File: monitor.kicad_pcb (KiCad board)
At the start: 4 copper layers, 35.5 x 33.7 mm, 54 parts, among them J1 USB_C_Plug, J2 USB_C_Receptacle_USB2.0_14P, J3 Display, J4 Program, J5 Boot, U1 STM32U031K8Ux, U2 TPSM365R6V3RDNR, U3 TMP117xxDRV, U4 REF5025ADGK, U5 CC6903, Y1 32768Hz

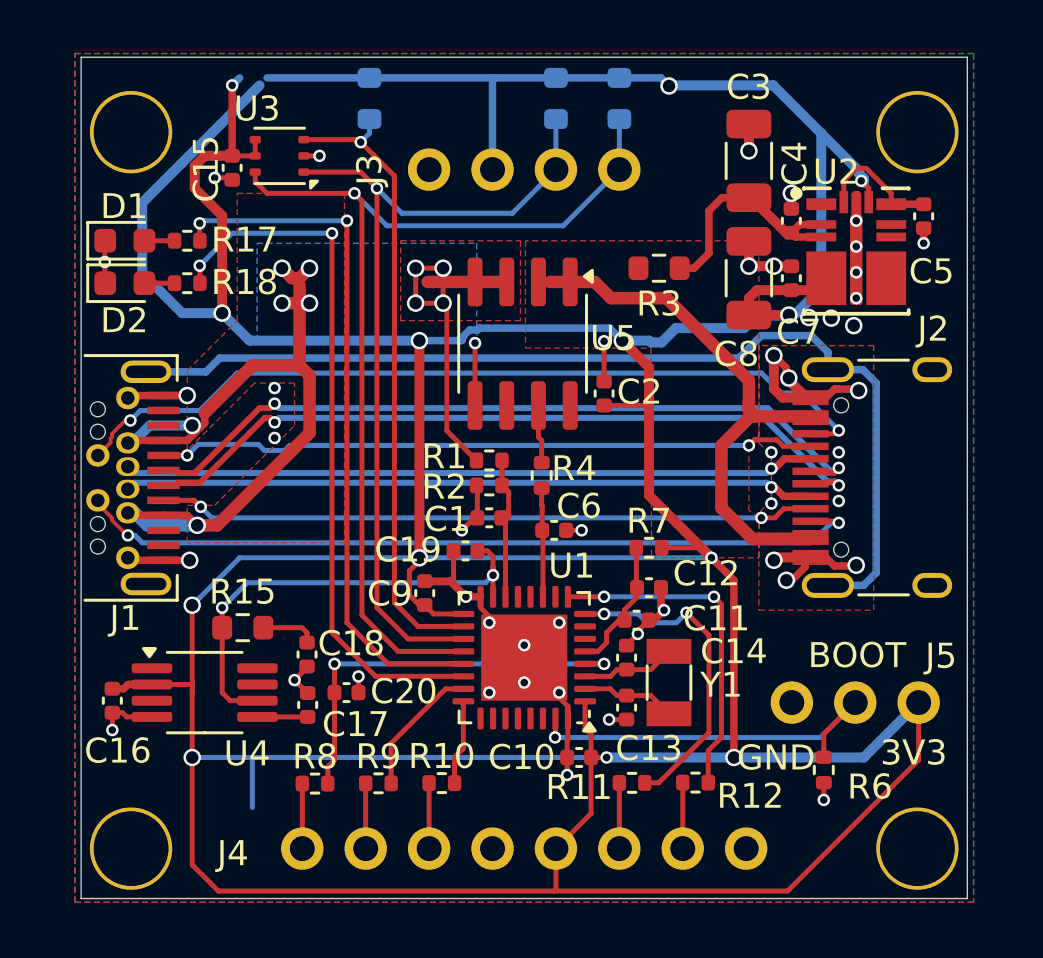
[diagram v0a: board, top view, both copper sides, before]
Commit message: Big update to the monitor.
Accell, low side current sense.
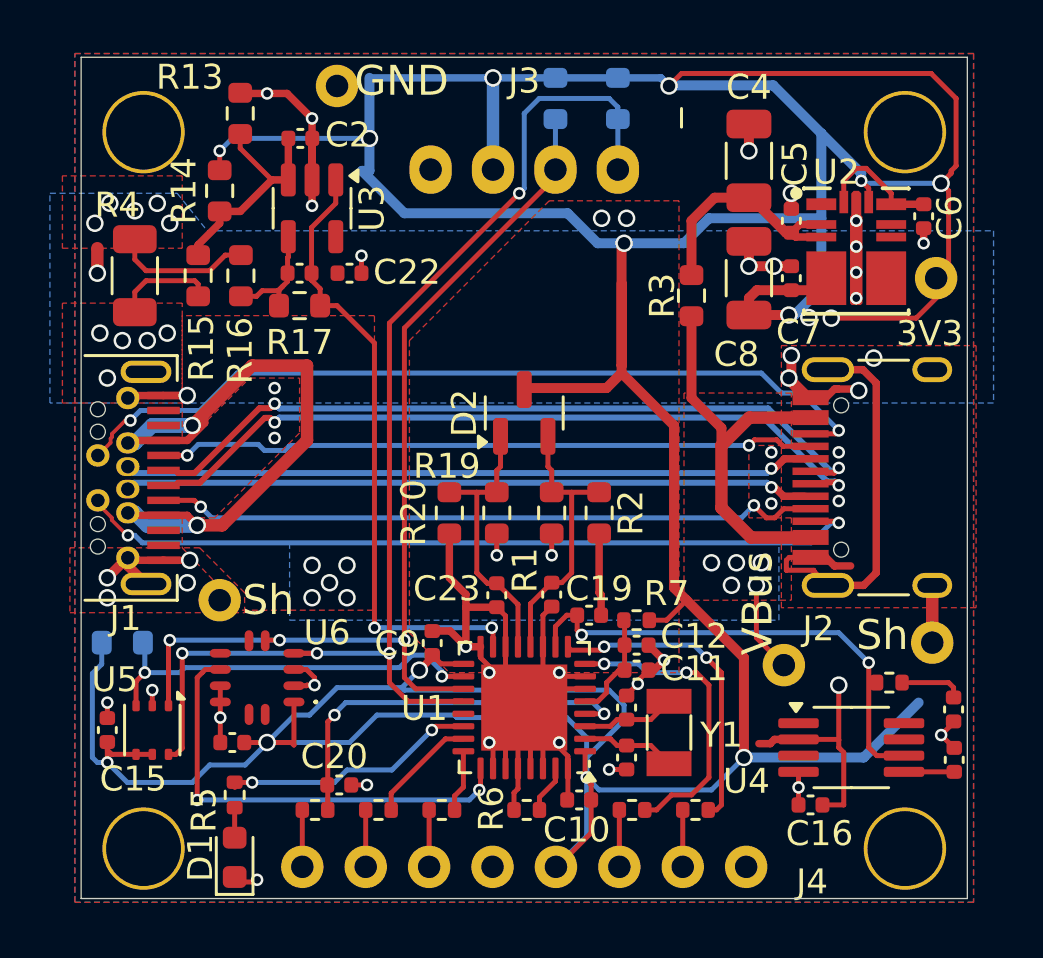
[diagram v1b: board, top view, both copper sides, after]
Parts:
- removed the C6 at (101.2, 102.1)
- removed J5: Boot, Parts:PinHeader_1x03_P2.54mm_Vertical
- removed the R18 at (86.5, 92.2)
- removed the U5 at (99.9, 94.6)
- added C21: 1u, Capacitor_SMD:C_0402_1005Metric, F.Cu at (88.3, 110.6)
- added C22: 0u1, Capacitor_SMD:C_0402_1005Metric, F.Cu at (93.0, 91.8)
- added C23: 4u7, Capacitor_SMD:C_0402_1005Metric, F.Cu at (98.9, 104.7)
- added C3: 1u, Capacitor_SMD:C_0402_1005Metric, F.Cu at (91.0, 91.8)
- added NT1: NetTie_2, Parts:NetTie-2_0.2mm, F.Cu at (84.4, 92.7)
- added NT2: NetTie_2, Parts:NetTie-2_0.2mm, F.Cu at (84.4, 91.1)
- added NT3: NetTie_2, NetTie:NetTie-2_SMD_Pad0.5mm, F.Cu at (82.9, 91.3)
- added R13: 200k, Resistor_SMD:R_0603_1608Metric, F.Cu at (88.6, 85.4)
- added R14: 200k, Resistor_SMD:R_0603_1608Metric, F.Cu at (87.8, 88.5)
- added R15: 390, Resistor_SMD:R_0603_1608Metric, F.Cu at (86.9, 91.9)
- added R16: 390, Resistor_SMD:R_0603_1608Metric, F.Cu at (88.7, 91.9)
- added R17: 100k, Resistor_SMD:R_0603_1608Metric, F.Cu at (91.0, 93.1)
- added R19: 330k, Resistor_SMD:R_0603_1608Metric, F.Cu at (98.9, 101.4)
- added R20: 22k, Resistor_SMD:R_0603_1608Metric, F.Cu at (97.0, 101.4)
- added TP1: TestPoint, Parts:TestPoint, F.Cu at (87.8, 104.9)
- added TP2: TestPoint, Parts:TestPoint, F.Cu at (116.3, 106.6)
- added TP3: TestPoint, Parts:TestPoint, F.Cu at (110.4, 107.5)
- added TP4: TestPoint, Parts:TestPoint, F.Cu at (92.5, 84.3)
- added TP5: TestPoint, Parts:TestPoint, F.Cu at (116.5, 92.0)
- added U3: OPA388, Package_TO_SOT_SMD:SOT-23-5, F.Cu at (91.5, 89.2)
- added U6: FXLS8971CF, Parts:FXLS8971CF, F.Cu at (89.3, 108.0)
- C1: value 10u -> 1u
- C2: value 0u1 -> 1u
- C20: value 0u1 -> 100p
- D2: value Red -> BAV70; footprint LED_SMD:LED_0603_1608Metric -> Package_TO_SOT_SMD:SOT-23
- H1, H3, H4: moved to B.Cu
- J3: footprint Parts:PinHeader_1x04_P2.54mm_Vertical -> Parts:JST_XH_B4B-XH-A_1x04_P2.50mm_Vertical
- R1: value 100k -> 220k; footprint Resistor_SMD:R_0402_1005Metric -> Resistor_SMD:R_0603_1608Metric
- R18: renamed from R15; footprint Resistor_SMD:R_0603_1608Metric -> Resistor_SMD:R_0402_1005Metric
- R2: value 18k -> 100k; footprint Resistor_SMD:R_0402_1005Metric -> Resistor_SMD:R_0603_1608Metric
- R4: value 220 -> 1m; footprint Resistor_SMD:R_0402_1005Metric -> Resistor_SMD:R_1206_3216Metric
- moved C16 28.3 mm to (111.5, 113.1), turned to 180 degrees
- moved C18 26.0 mm to (117.2, 109.3)
- moved R18 26.0 mm to (114.6, 108.2)
- moved C17 26.0 mm to (117.2, 111.3)
- moved U4 26.0 mm to (113.1, 110.8)
- moved D1 25.1 mm to (88.4, 115.2), turned to 90 degrees
- moved R33 23.9 mm to (83.9, 106.6), turned to 0 degrees
- moved U5 23.6 mm to (85.1, 110.1), turned to -90 degrees
- moved C15 23.1 mm to (83.3, 110.1), turned to 90 degrees
- moved R5 22.3 mm to (88.4, 112.7), turned to -90 degrees
- moved R4 18.2 mm to (84.4, 91.9), turned to -90 degrees
- moved D2 16.8 mm to (100.0, 97.4), turned to 90 degrees
- moved C2 15.9 mm to (91.0, 86.4), turned to 180 degrees
- moved R6 12.0 mm to (100.1, 113.3), turned to 0 degrees
- moved C19 5.58 mm to (102.6, 105.5), turned to 0 degrees
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- renumbered C3 to C4, C4 to C5, C5 to C6, R13 to R31, R14 to R32, R5 to R33, R17 to R5, U3 to U5
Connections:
- C1 pad 1: /VSense -> /VSense1
- C2 pad 1: +3V3 -> GND
- C2 pad 2: GND -> Net-(U3-+)
- D2 pad 1: GND -> /VSense2
- D2 pad 2: Net-(D2-A) -> /VSense1
- J1 pad A1: GND -> /MGnd
- J1 pad A12: GND -> /MGnd
- J1 pad A4: /Vout -> /VBus
- J1 pad A9: /Vout -> /VBus
- J1 pad B1: GND -> /MGnd
- J1 pad B12: GND -> /MGnd
- J1 pad B4: /Vout -> /VBus
- J1 pad B9: /Vout -> /VBus
- J1 pad S1: unconnected-(J1-SHIELD-PadS1) -> /MGnd
- J1 pad S2: Earth -> /MGnd
- J2 pad A1: GND -> /UGnd
- J2 pad A12: GND -> /UGnd
- J2 pad B1: GND -> /UGnd
- J2 pad B12: GND -> /UGnd
- J2 pad S1: Earth -> /UGnd
- J2 pad S2: unconnected-(J2-SHIELD-PadS2) -> /UGnd
- J2 pad S3: unconnected-(J2-SHIELD-PadS3) -> /UGnd
- J2 pad S4: Earth -> /UGnd
- R1 pad 1: /Vout -> /VBus
- R1 pad 2: /VSense -> /VSense1
- R2 pad 1: /VSense -> GND
- R2 pad 2: GND -> /VSense1
- R4 pad 1: /ISense -> /UGnd
- R4 pad 2: Net-(U5-VIOUT) -> /MGnd
- R5 pad 1: /Green -> /White
- R6 pad 1: /BOOT0 -> GND
- R6 pad 2: GND -> /BOOT0
- U1 pad 10: unconnected-(U1-PA4-Pad10) -> /VRef
- U1 pad 11: /ISense -> GND
- U1 pad 12: unconnected-(U1-PA6-Pad12) -> /VSense1
- U1 pad 13: unconnected-(U1-PA7-Pad13) -> /VSense2
- U1 pad 14: /VSense -> GND
- U1 pad 15: /VRef -> /ISense
- U1 pad 21: /Green -> unconnected-(U1-PA11-Pad21)
- U1 pad 22: /Red -> /White
- U1 pad 25: unconnected-(U1-PA15-Pad25) -> /AccInt
- U1 pad 26: unconnected-(U1-PB3-Pad26) -> GND
- U1 pad 27: unconnected-(U1-PB4-Pad27) -> GND
- U1 pad 28: unconnected-(U1-PB5-Pad28) -> GND
- U1 pad 29: unconnected-(U1-PB6-Pad29) -> GND
- U1 pad 30: unconnected-(U1-PB7-Pad30) -> GND
- U1 pad 6: unconnected-(U1-PA0-Pad6) -> GND
- U1 pad 7: unconnected-(U1-PA1-Pad7) -> GND
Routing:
- net /Vout: track 46.4 -> 0.00 mm, vias 10 -> 0
- net Earth: track 40.8 -> 0.00 mm
- net /Red: track 28.5 -> 0.00 mm, vias 2 -> 0
- net /Green: track 28.1 -> 0.00 mm, vias 2 -> 0
- net /VBus: track 21.8 -> 48.3 mm, vias 0 -> 14
- net /MGnd: track 0.00 -> 26.4 mm, vias 0 -> 10
- net /UGnd: track 0.00 -> 24.6 mm, vias 0 -> 9
- net GND: track 48.1 -> 71.6 mm, vias 45 -> 38
- net /ISense: track 4.33 -> 25.3 mm, vias 0 -> 2
- net /AccInt: track 0.00 -> 18.3 mm, vias 0 -> 2
- net +3V3: track 240.0 -> 222.2 mm
- net /BOOT0: track 16.1 -> 1.93 mm, vias 1 -> 0
- net /VSense1: track 0.00 -> 11.1 mm
- net /VSense2: track 0.00 -> 11.1 mm
- net /White: track 0.00 -> 10.1 mm, vias 0 -> 2
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- added copper zone on F.Cu, net /MGnd
- added copper zone on In1.Cu, net /MGnd
- added copper zone on B.Cu, net /UGnd
- added copper zone on F.Cu, net /UGnd
- added copper zone on B.Cu, net /VBus
- removed copper zone on B.Cu, net /Vout
- removed copper zone on F.Cu, net /Vout
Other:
- board text added: "Sh"
- board text added: "VBus"
- board text removed: "BOOT"

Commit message: Switch to the 2-stage sense amp.
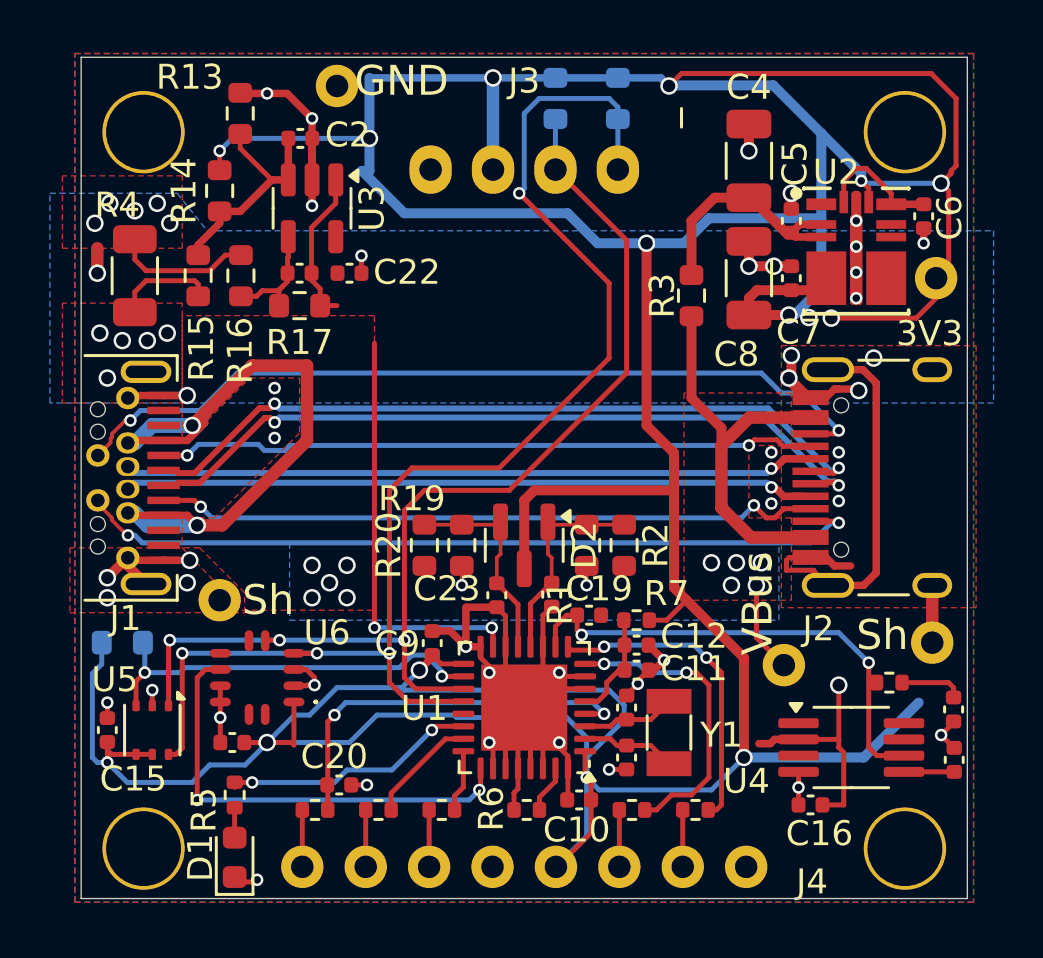
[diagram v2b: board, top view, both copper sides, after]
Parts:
- moved D2 5.30 mm to (100.0, 102.7), turned to -90 degrees
- moved R1 1.91 mm to (102.5, 102.7)
- moved R19 1.91 mm to (97.5, 102.7)
- moved R2 1.64 mm to (104.0, 102.7)
- moved R20 1.64 mm to (96.0, 102.7)
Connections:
- D2 pad 1: /VSense2 -> /VSense1
- D2 pad 2: /VSense1 -> /VSense2
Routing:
- net GND: track 71.6 -> 65.2 mm, vias 38 -> 36
- net /SDA: track 48.6 -> 53.6 mm
- net /SCL: track 40.1 -> 44.4 mm
- net /VSense1: track 11.1 -> 8.51 mm
- net /VSense2: track 11.1 -> 8.51 mm
- net /ISense: track 25.3 -> 23.1 mm
- net +3V3: track 222.2 -> 223.1 mm
- removed copper zone on F.Cu, net GND

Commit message: Board layout updated.
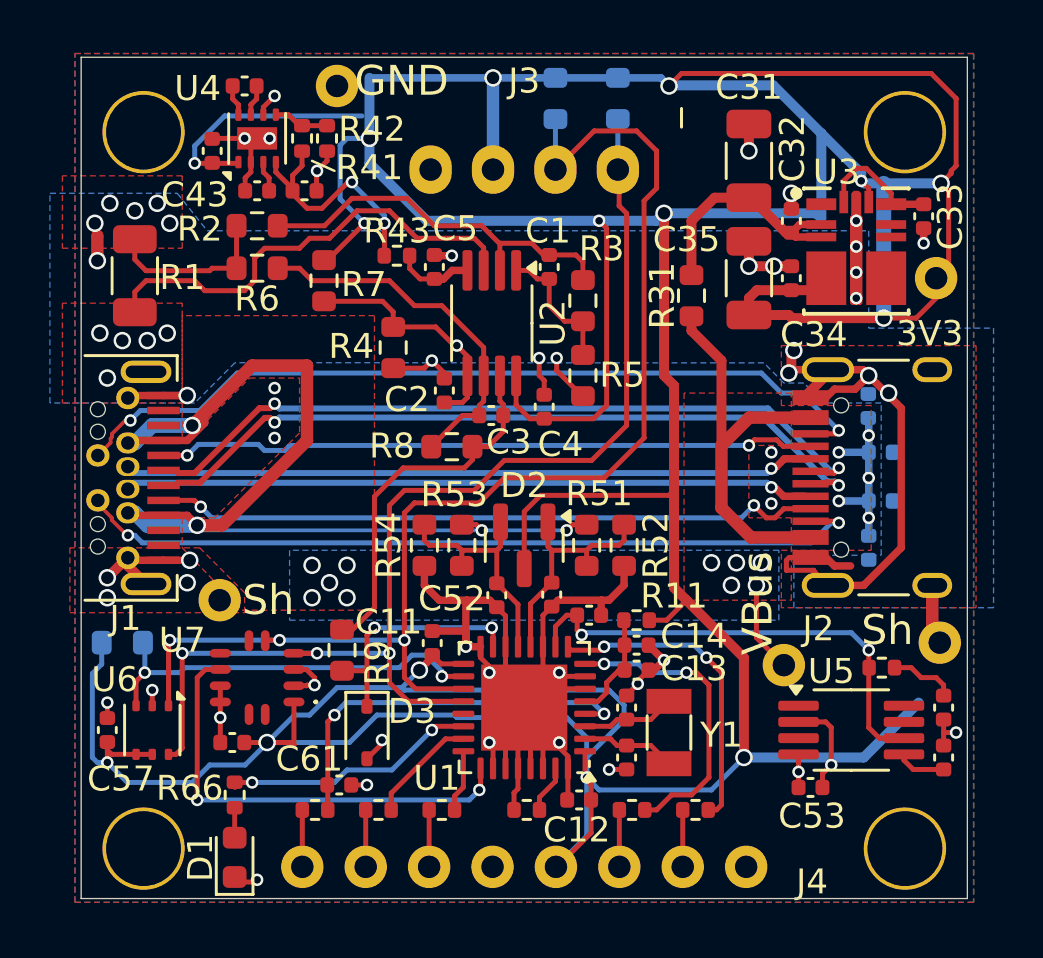
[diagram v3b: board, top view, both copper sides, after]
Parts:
- removed C22: 0u1, Capacitor_SMD:C_0402_1005Metric
- removed R15, R16: 390, Resistor_SMD:R_0603_1608Metric
- removed the U3 at (91.5, 89.2)
- added C2: 1u, Capacitor_SMD:C_0402_1005Metric, F.Cu at (96.8, 96.5)
- added C4: 0u1, Capacitor_SMD:C_0402_1005Metric, F.Cu at (100.8, 97.2)
- added C41: 4u7, Capacitor_SMD:C_0402_1005Metric, F.Cu at (87.5, 86.9)
- added C42: 1u, Capacitor_SMD:C_0402_1005Metric, F.Cu at (88.8, 84.3)
- added C43: 4u7, Capacitor_SMD:C_0402_1005Metric, F.Cu at (89.3, 88.5)
- added C44: 4u7, Capacitor_SMD:C_0402_1005Metric, F.Cu at (91.2, 88.5)
- added C5: 0u1, Capacitor_SMD:C_0402_1005Metric, F.Cu at (96.4, 91.5)
- added C91: 0u1, Capacitor_SMD:C_0402_1005Metric, B.Cu at (113.8, 102.8)
- added C92: 0u1, Capacitor_SMD:C_0402_1005Metric, B.Cu at (114.3, 99.0)
- added C93: 0u1, Capacitor_SMD:C_0402_1005Metric, B.Cu at (114.3, 100.9)
- added C94: 0u1, Capacitor_SMD:C_0402_1005Metric, B.Cu at (113.8, 97.1)
- added D3: 1N5819, Diode_SMD:D_SOD-323, F.Cu at (93.7, 110.2)
- added R2: 1k, Resistor_SMD:R_0603_1608Metric, F.Cu at (89.3, 89.9)
- added R41: 200k, Resistor_SMD:R_0402_1005Metric, F.Cu at (91.1, 86.4)
- added R42: 510k, Resistor_SMD:R_0402_1005Metric, F.Cu at (92.1, 86.4)
- added R43: 10, Resistor_SMD:R_0402_1005Metric, F.Cu at (94.9, 91.1)
- added R5: 39k, Resistor_SMD:R_0603_1608Metric, F.Cu at (102.3, 95.9)
- added R6: 39k, Resistor_SMD:R_0603_1608Metric, F.Cu at (89.3, 91.6)
- added R8: 100k, Resistor_SMD:R_0603_1608Metric, F.Cu at (97.1, 98.8)
- added R9: 10, Resistor_SMD:R_0603_1608Metric, F.Cu at (92.7, 106.9)
- added U2: OPA2388, Package_SO:MSOP-8_3x3mm_P0.65mm, F.Cu at (98.7, 93.8)
- added U4: LM27761, Package_SON:WSON-8-1EP_2x2mm_P0.5mm_EP0.9x1.6mm, F.Cu at (89.3, 86.4)
- moved C3 13.5 mm to (98.7, 97.5)
- moved R3 11.4 mm to (102.3, 92.9), turned to -90 degrees
- moved R4 11.2 mm to (94.8, 94.8), turned to 90 degrees
- moved C1 10.0 mm to (101.0, 91.5), turned to 90 degrees
- moved R7 5.52 mm to (92.0, 92.1)
- moved U5 0.70 mm to (113.1, 110.1)
- moved C53 0.70 mm to (111.5, 112.4)
- moved R55 0.67 mm to (114.3, 107.6)
- moved NT3 0.50 mm to (82.9, 90.8)
- moved C54 0.44 mm to (116.8, 111.2)
- moved C55 0.41 mm to (116.8, 109.2)
- moved TP2 0.30 mm to (116.6, 106.6)
- turned R51 to -90 degrees
- turned R53 to -90 degrees
- renumbered C3 to C1, C9 to C11, C10 to C12, C11 to C13, C12 to C14, C13 to C16, C14 to C17, C2 to C3, C4 to C31, C5 to C32, C6 to C33, C7 to C34, C8 to C35, C1 to C51, C23 to C52, C16 to C53, C17 to C54, C18 to C55, C19 to C56, C15 to C57, C21 to C58, C20 to C61, R4 to R1, R7 to R11, R6 to R12, R17 to R3, R3 to R31, R13 to R4, R1 to R51, R2 to R52, R19 to R53, R20 to R54, R18 to R55, R31 to R56, R32 to R57, R33 to R58, R8 to R61, R9 to R62, R10 to R63, R11 to R64, R12 to R65, R5 to R66, R14 to R7, TP4 to TP301, TP5 to TP31, U2 to U3, U4 to U5, U5 to U6, U6 to U7
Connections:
- net Net-(U3--) renamed /A1-
- C1 pad 1: /ISense -> /A1
- C3 pad 1: GND -> /ISense
- C3 pad 2: Net-(U3-+) -> /A2-
- R3 pad 2: /ISense -> /A1
- R4 pad 2: Net-(U3-+) -> /A2+
- R7 pad 1: Net-(U3-+) -> /A2+
- U1 pad 15: /ISense -> /ISenseP
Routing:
- net +3V3: track 223.1 -> 243.1 mm, vias 16 -> 17
- net /A2+: track 0.00 -> 15.9 mm, vias 0 -> 2
- net /VBus: track 48.1 -> 63.2 mm
- net /A2-: track 0.00 -> 14.8 mm
- net /ISense+: track 3.27 -> 17.7 mm
- net /A1-: track 4.76 -> 15.5 mm
- net /-1V7: track 0.00 -> 9.63 mm, vias 0 -> 2
- net /ISenseP: track 0.00 -> 9.53 mm, vias 0 -> 2
- net Net-(U3-+): track 9.40 -> 0.00 mm
- net /ISense: track 23.1 -> 14.9 mm, vias 2 -> 0
- net /SCL: track 44.4 -> 51.3 mm
- net /SDA: track 53.6 -> 47.2 mm, vias 4 -> 3
- net /MGnd: track 26.4 -> 32.0 mm, vias 10 -> 19
- net /A1: track 0.00 -> 5.50 mm
- net /-1V7F: track 0.00 -> 3.14 mm
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- added copper zone on In2.Cu, net /MGnd
- added copper zone on In1.Cu, net /UGnd
- added copper zone on In2.Cu, net /UGnd
- added copper zone on In2.Cu, net /VBus

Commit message: Tweaks.  Fabbing.
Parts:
- R9: footprint Resistor_SMD:R_0603_1608Metric -> Resistor_SMD:R_0402_1005Metric
- moved R9 0.57 mm to (93.1, 106.5)
